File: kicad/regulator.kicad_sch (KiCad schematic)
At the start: 3 parts, among them U501 ADP122 1.8V

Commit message: Added Digikey references
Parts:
- C501, C505: Digikey (none) -> 399-C0402C105K9PAC7800CT-ND
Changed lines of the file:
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@@
       (effects (font (size 1.27 1.27)) hide)
     )
-    (property "Datasheet" "https://product.tdk.com/info/en/catalog/datasheets/mlcc_commercial_general_en.pdf" (id 3) (at 114.3 105.41 0)
+    (property "Datasheet" "~" (id 3) (at 114.3 105.41 0)
       (effects (font (size 1.27 1.27)) hide)
     )
-    (property "Digikey" "" (id 4) (at 114.3 105.41 0)
+    (property "Digikey" "399-C0402C105K9PAC7800CT-ND" (id 4) (at 114.3 105.41 0)
       (effects (font (size 1.27 1.27)) hide)
     )
@@
       (effects (font (size 1.27 1.27)) hide)
     )
-    (property "Datasheet" "https://product.tdk.com/info/en/catalog/datasheets/mlcc_commercial_general_en.pdf" (id 3) (at 144.78 109.22 0)
+    (property "Datasheet" "~" (id 3) (at 144.78 109.22 0)
       (effects (font (size 1.27 1.27)) hide)
     )
-    (property "Digikey" "" (id 4) (at 144.78 109.22 0)
+    (property "Digikey" "399-C0402C105K9PAC7800CT-ND" (id 4) (at 144.78 109.22 0)
       (effects (font (size 1.27 1.27)) hide)
     )

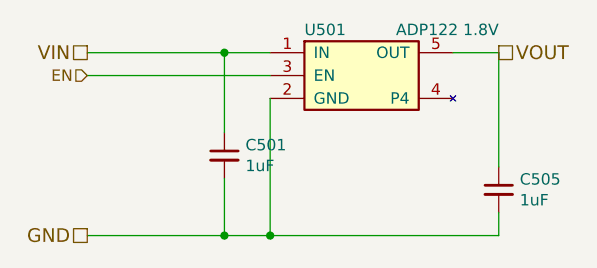
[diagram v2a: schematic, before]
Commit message: One shining moment
Commit board while it still works
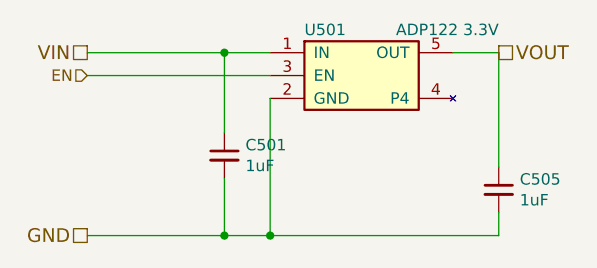
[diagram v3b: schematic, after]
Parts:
- U501: value ADP122 1.8V -> ADP122 3.3V; Purpose Regulator -> Regulator VBus->3.3V
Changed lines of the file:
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@@
       (effects (font (size 1.27 1.27)) (justify left))
     )
-    (property "Value" "ADP122 1.8V" (id 1) (at 144.78 91.44 0)
+    (property "Value" "ADP122 3.3V" (id 1) (at 144.78 91.44 0)
       (effects (font (size 1.27 1.27)) (justify right))
     )
@@
       (effects (font (size 1.27 1.27)) hide)
     )
-    (property "Purpose" "Regulator" (id 5) (at 129.54 96.52 0)
+    (property "Purpose" "Regulator VBus->3.3V" (id 5) (at 129.54 96.52 0)
       (effects (font (size 1.27 1.27)) hide)
     )

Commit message: Updated part number
Darn supply chain crisis :(
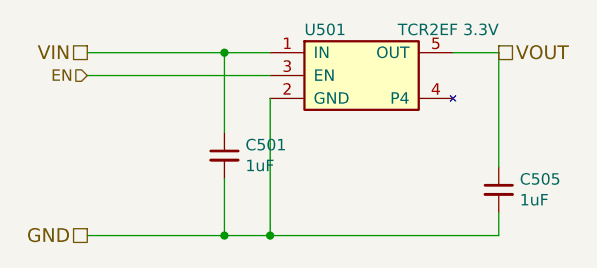
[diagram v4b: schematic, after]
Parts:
- U501: value ADP122 3.3V -> TCR2EF 3.3V; Digikey 505-ADP122AUJZ-3.3-R7CT-ND -> TCR2EF33LM(CTCT-ND
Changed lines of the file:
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@@
       (effects (font (size 1.27 1.27)) (justify left))
     )
-    (property "Value" "ADP122 3.3V" (id 1) (at 144.78 91.44 0)
+    (property "Value" "TCR2EF 3.3V" (id 1) (at 144.78 91.44 0)
       (effects (font (size 1.27 1.27)) (justify right))
     )
@@
       (effects (font (size 1.27 1.27)) hide)
     )
-    (property "Digikey" "505-ADP122AUJZ-3.3-R7CT-ND" (id 4) (at 129.54 96.52 0)
+    (property "Digikey" "TCR2EF33LM(CTCT-ND" (id 4) (at 129.54 96.52 0)
       (effects (font (size 1.27 1.27)) hide)
     )

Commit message: Updated purposes for regulators
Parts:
- C501: Purpose Regulator Input -> 3.3V Regulator Input
- C505: Purpose Shoulder Regulator output -> 3.3V Regulator output
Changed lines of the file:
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@@
       (effects (font (size 1.27 1.27)) hide)
     )
-    (property "Purpose" "Regulator Input" (id 5) (at 114.3 105.41 0)
+    (property "Purpose" "3.3V Regulator Input" (id 5) (at 114.3 105.41 0)
       (effects (font (size 1.27 1.27)) hide)
     )
@@
       (effects (font (size 1.27 1.27)) hide)
     )
-    (property "Purpose" "Shoulder Regulator output" (id 5) (at 144.78 109.22 0)
+    (property "Purpose" "3.3V Regulator output" (id 5) (at 144.78 109.22 0)
       (effects (font (size 1.27 1.27)) hide)
     )

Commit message: Checkin before branch
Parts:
- renumbered C501 to C401, C505 to C405, U501 to U401
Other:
- company: (none) -> Kwan Systems
- title: (none) -> Rollercoasterometer
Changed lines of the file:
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@@
 (kicad_sch (version 20211123) (generator eeschema)
-  (paper "A4")
+  (paper "USLetter")
+  (title_block
+    (title "Rollercoasterometer")
+    (date "2022-10-07")
+    (company "Kwan Systems")
+  )
   (junction (at 114.3 93.98) (diameter 0) (color 0 0 0 0)
   )
@@
   (symbol (lib_id "KwanSystems:ADP122") (at 129.54 96.52 0) (unit 1)
     (in_bom yes) (on_board yes)
-    (property "Reference" "U501" (id 0) (at 123.19 91.44 0)
+    (property "Reference" "U401" (id 0) (at 123.19 91.44 0)
       (effects (font (size 1.27 1.27)) (justify left))
     )
@@
   (symbol (lib_id "Device:C_Small") (at 114.3 105.41 0) (unit 1)
     (in_bom yes) (on_board yes)
-    (property "Reference" "C501" (id 0) (at 116.6368 104.2416 0)
+    (property "Reference" "C401" (id 0) (at 116.6368 104.2416 0)
       (effects (font (size 1.27 1.27)) (justify left))
     )
@@
   (symbol (lib_id "Device:C_Small") (at 144.78 109.22 0) (unit 1)
     (in_bom yes) (on_board yes)
-    (property "Reference" "C505" (id 0) (at 147.1168 108.0516 0)
+    (property "Reference" "C405" (id 0) (at 147.1168 108.0516 0)
       (effects (font (size 1.27 1.27)) (justify left))
     )

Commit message: Commit as-ordered shipometer 23.03
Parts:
- C401, C405: Mouser (none) -> 187-CL05A105KP5NNWC; Number on hand (none) -> 14+10
- U401: Number on hand (none) -> 1
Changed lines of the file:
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@@
+      (effects (font (size 1.27 1.27)) hide)
+    )
+    (property "Number on hand" "1" (id 6) (at 129.54 96.52 0)
       (effects (font (size 1.27 1.27)) hide)
     )
@@
     )
     (property "Purpose" "3.3V Regulator Input" (id 5) (at 114.3 105.41 0)
+      (effects (font (size 1.27 1.27)) hide)
+    )
+    (property "Mouser" "187-CL05A105KP5NNWC" (id 6) (at 114.3 105.41 0)
+      (effects (font (size 1.27 1.27)) hide)
+    )
+    (property "Number on hand" "14+10" (id 7) (at 114.3 105.41 0)
       (effects (font (size 1.27 1.27)) hide)
     )
@@
       (effects (font (size 1.27 1.27)) hide)
     )
+    (property "Mouser" "187-CL05A105KP5NNWC" (id 9) (at 144.78 109.22 0)
+      (effects (font (size 1.27 1.27)) hide)
+    )
+    (property "Number on hand" "14+10" (id 10) (at 144.78 109.22 0)
+      (effects (font (size 1.27 1.27)) hide)
+    )
